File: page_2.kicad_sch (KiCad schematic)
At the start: 32 parts, among them J3 Conn_01x05, SW1 SW_Push, SW2 SW_Push, T201 TP 201, U3 TCA9535PWR, U4 TCA9535PWR

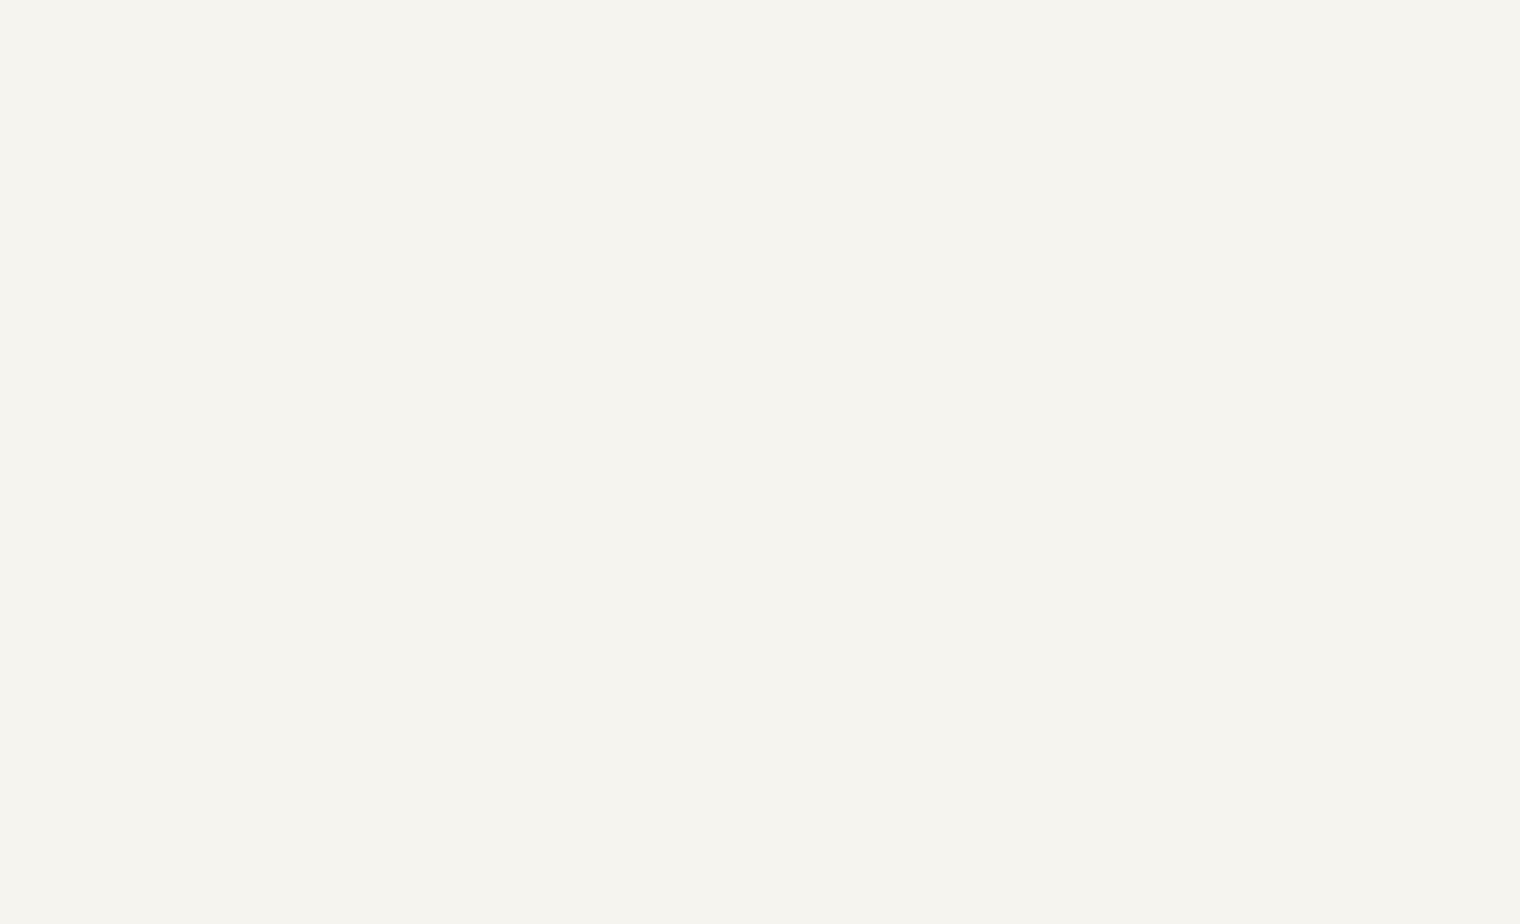
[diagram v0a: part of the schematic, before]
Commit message: Add USB-C interface and protection
This change replaces the generic 5-pin connector with a USB-C receptacle symbol and the corresponding USB 2.0 pin mapping. It also adds the associated protection and power-path components, including ESD protection, a fuse, and supporting passives, while updating the surrounding net labels and sheet symbols to reflect the new USB connectivity.
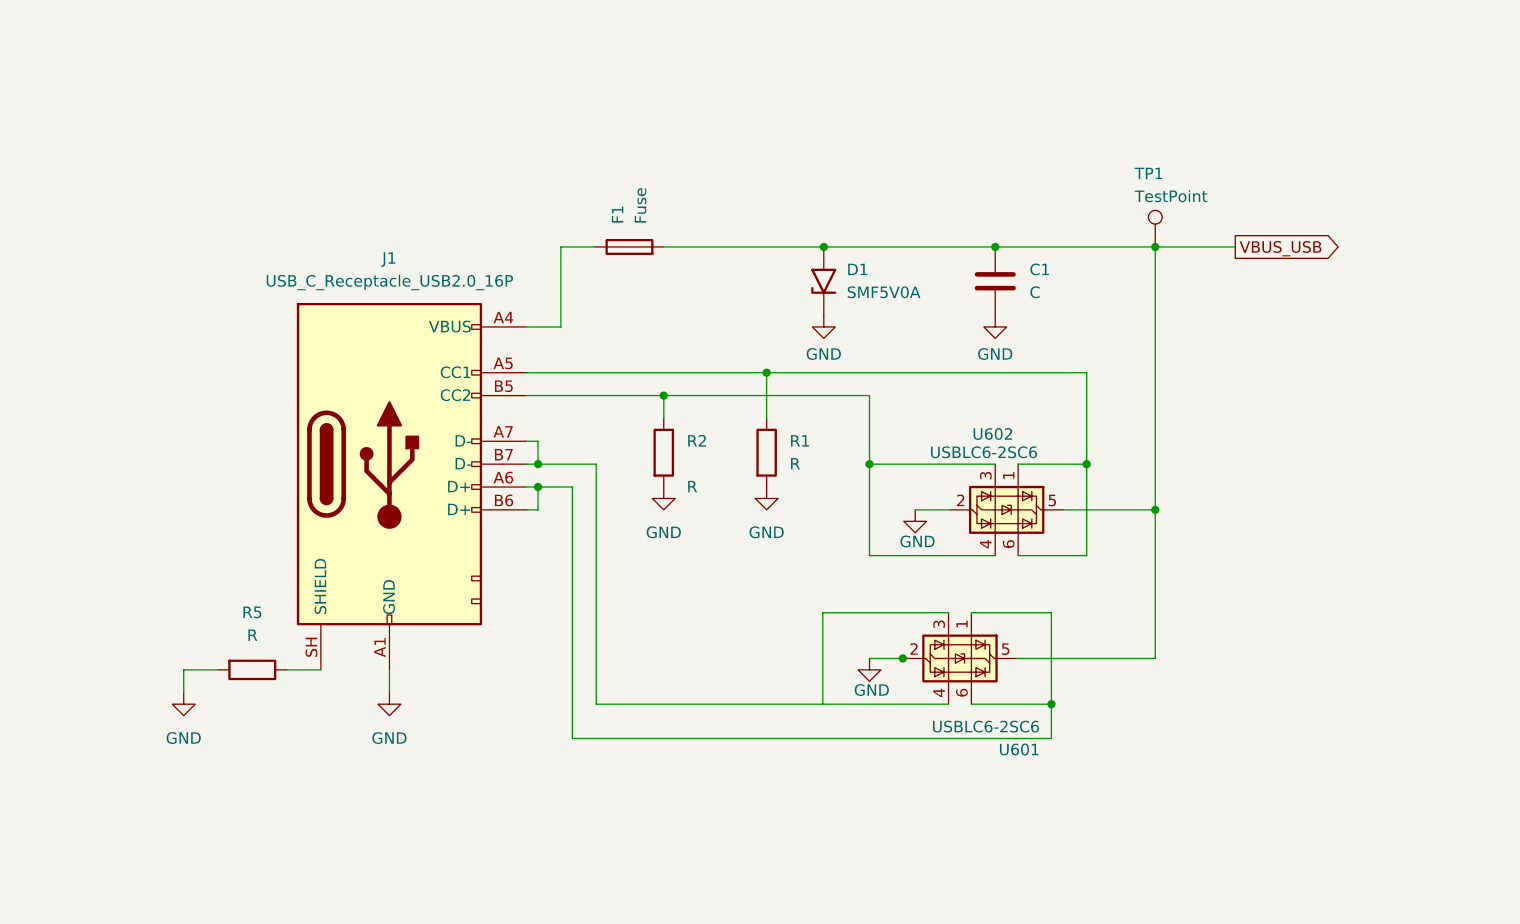
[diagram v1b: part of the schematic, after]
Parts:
- added C1: C, symbol Device:C
- added D1: SMF5V0A, Diode_SMD:D_SMF, symbol Diode:SMF5V0A
- added F1: Fuse, Package_LCC:PLCC-84_29.3x29.3mm_P1.27mm, symbol Device:Fuse
- added J1: USB_C_Receptacle_USB2.0_16P, Package_DFN_QFN:WDFN-10-1EP_3x3mm_P0.5mm_EP1.8x2.5mm, symbol Connector:USB_C_Receptacle_USB2.0_16P
- added R1, R2, R5: R, Package_DIP:DIP-8_W7.62mm, symbol Device:R
- added TP1: TestPoint, symbol Connector:TestPoint
- added U601, U602: USBLC6-2SC6, Package_TO_SOT_SMD:SOT-23-6, symbol Power_Protection:USBLC6-2SC6
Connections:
- net GND: now also C1.2, D1.1 (A1), J1.A1 (GND), J1.A12 (GND), J1.B1 (GND), J1.B12 (GND), R1.2, R2.2, R5.2, U601.2 (GND), U602.2 (GND)
- new net: F1.1, J1.A4 (VBUS), J1.A9 (VBUS), J1.B4 (VBUS), J1.B9 (VBUS)
- new net: J1.A5 (CC1), R1.1, U602.1 (I/O1), U602.6 (I/O1)
- new net: J1.A6 (D+), J1.B6 (D+), U601.1 (I/O1), U601.6 (I/O1)
- new net: J1.A7 (D-), J1.B7 (D-), U601.4 (I/O2)
- new net: J1.B5 (CC2), R2.1, U602.3 (I/O2), U602.4 (I/O2)
- new net: J1.SH (SHIELD), R5.1
- new net VBUS_USB: C1.1, D1.2 (A2), F1.2, TP1.1, U601.5 (VBUS), U602.5 (VBUS)

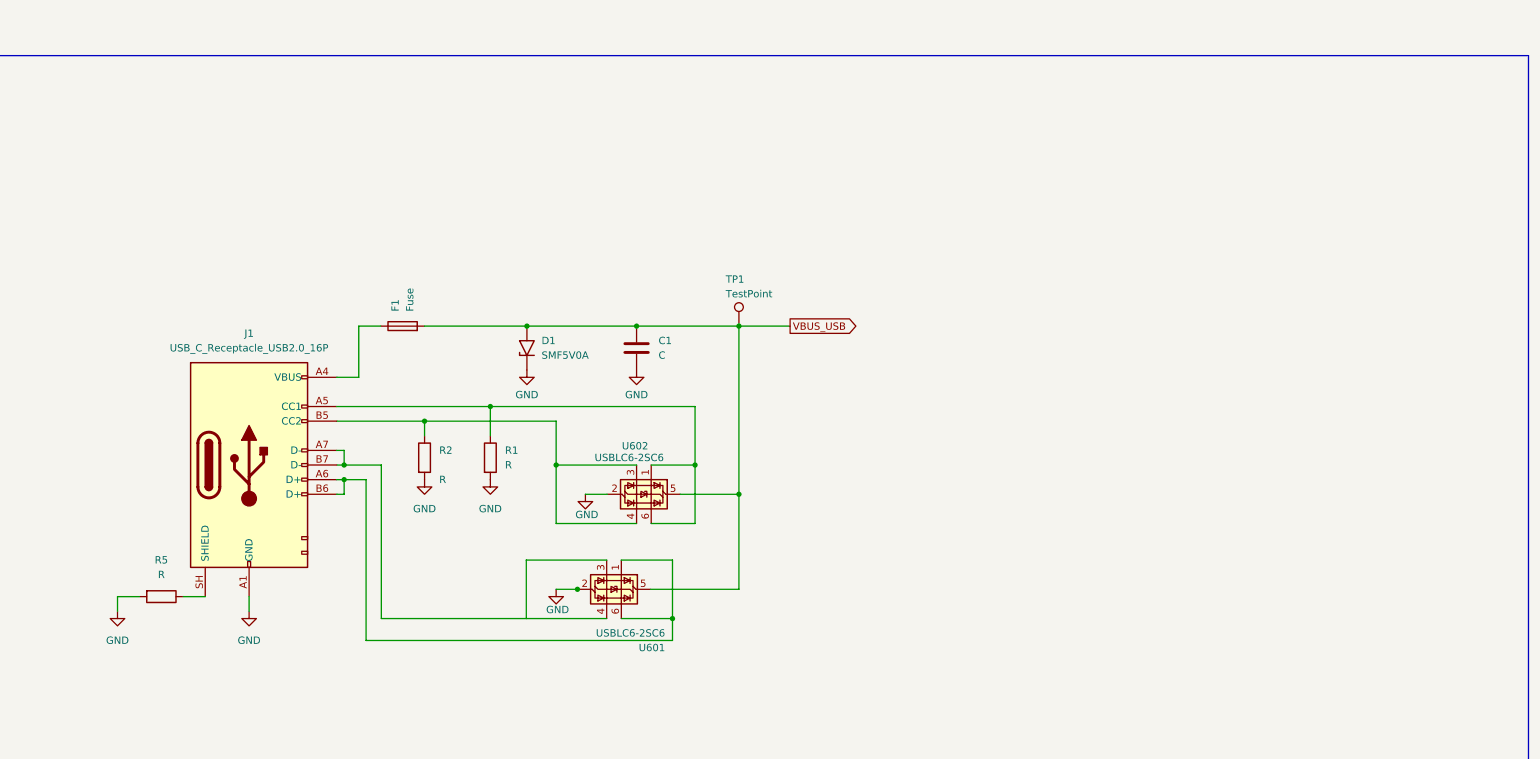
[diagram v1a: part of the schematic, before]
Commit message: Rework USB-C protection and net labels
This change repositions the USB-C connector and associated USB/CC net labels, rewires the VBUS and ESD protection path, and adds the required ground symbols and global labels for the USB interface. It also updates the related junctions and symbol references so the schematic matches the revised USB layout.
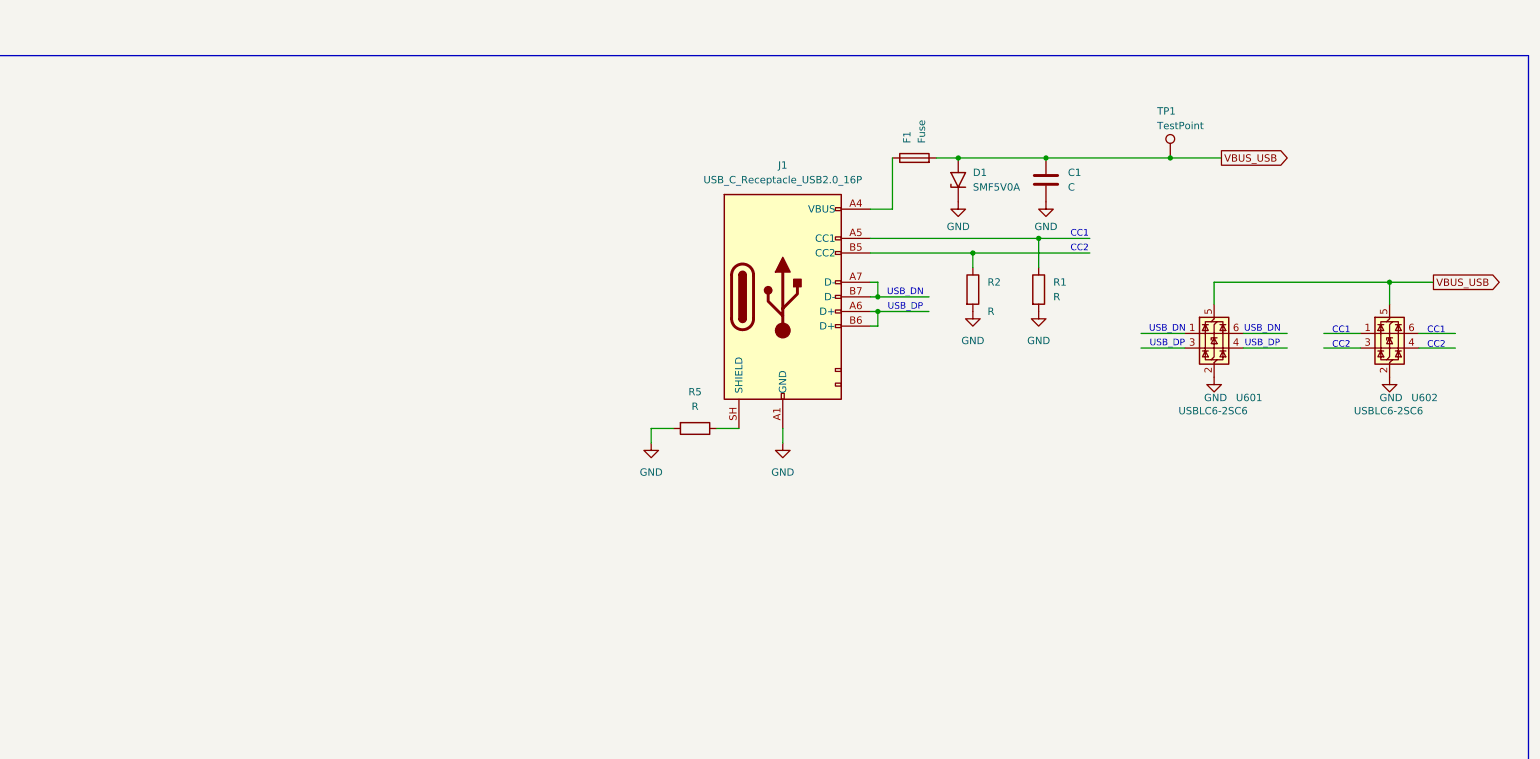
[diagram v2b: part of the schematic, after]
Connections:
- net at J1.A5 (CC1), R1.1: no longer U602.1 (I/O1), U602.6 (I/O1)
- net at J1.A6 (D+), J1.B6 (D+): no longer U601.1 (I/O1), U601.6 (I/O1)
- net at J1.A7 (D-), J1.B7 (D-): no longer U601.4 (I/O2)
- net at J1.B5 (CC2), R2.1: no longer U602.3 (I/O2), U602.4 (I/O2)
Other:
- note added: "CC1"
- note added: "CC2"
- note added: "USB_DN"
- note added: "USB_DP"
- moved on the sheet: C1, D1, F1, J1, R1, R2, R5, TP1

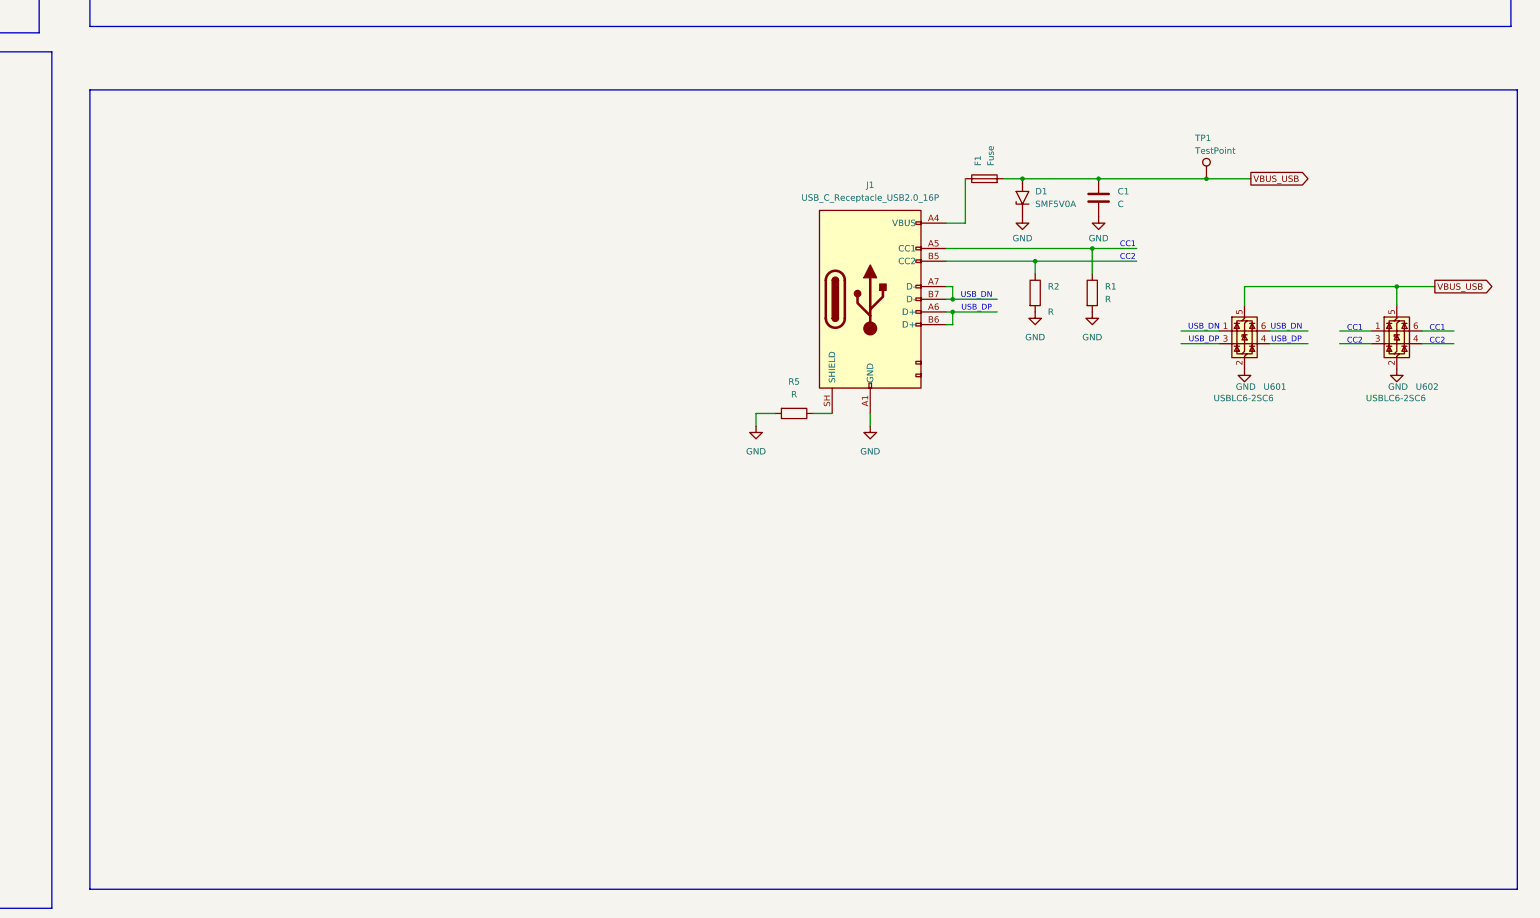
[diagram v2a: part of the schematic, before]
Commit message: Update USB-C receptacle schematic
This change refines the USB-C section in page_2 by updating the receptacle outline, adding the USB-C label, and correcting the wire/net geometry around the connector. It also renumbers the related components and test points, removes stale wiring/resistor entries, and updates the associated power and value annotations to match the final schematic layout.
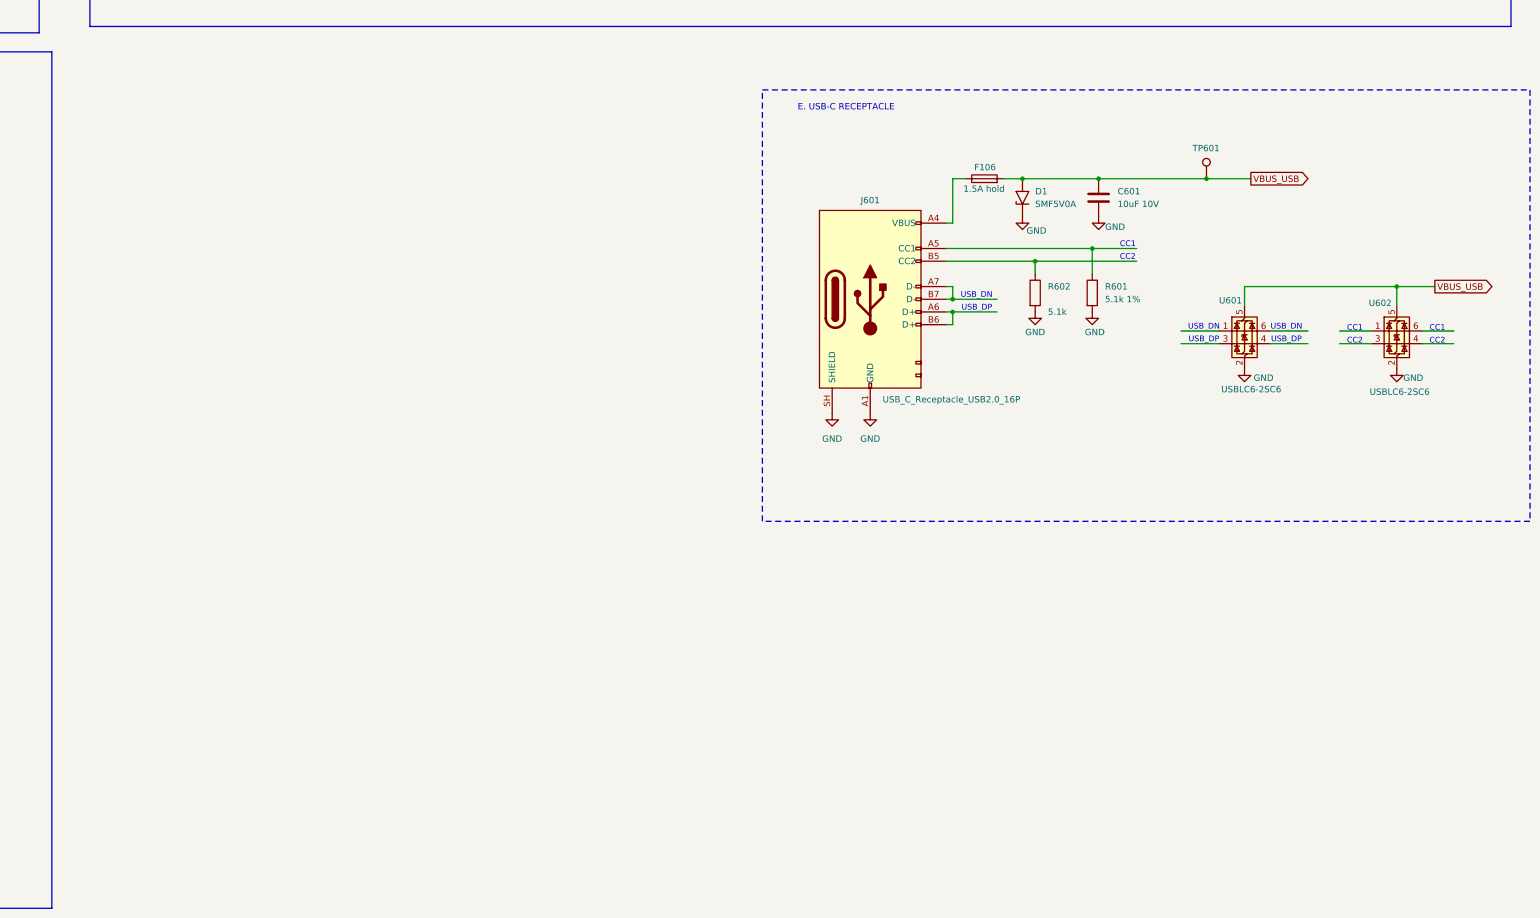
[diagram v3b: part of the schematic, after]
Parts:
- removed R5: R, Package_DIP:DIP-8_W7.62mm, symbol Device:R
- C601: renamed from C1; value C -> 10uF 10V
- F106: renamed from F1; value Fuse -> 1.5A hold
- R601: renamed from R1; value R -> 5.1k 1%
- R602: renamed from R2; value R -> 5.1k
- TP601: renamed from TP1; value TestPoint -> (none)
- renumbered J1 to J601
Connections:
- net GND: now also J601.SH (SHIELD)
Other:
- note added: "E. USB-C RECEPTACLE"
